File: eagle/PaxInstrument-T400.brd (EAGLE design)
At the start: 99.1 x 50.8 mm, 115 parts, among them IC1 MCP3424, J1 MICRO-SDCARD-CONNECTOR-330006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, U1 MCP9800, U3 MCP73831, U4 MIC5219-3.3V, U8 NC7S32, X1 FH12-12S-0.5SH, Y1 RESONATORSMD

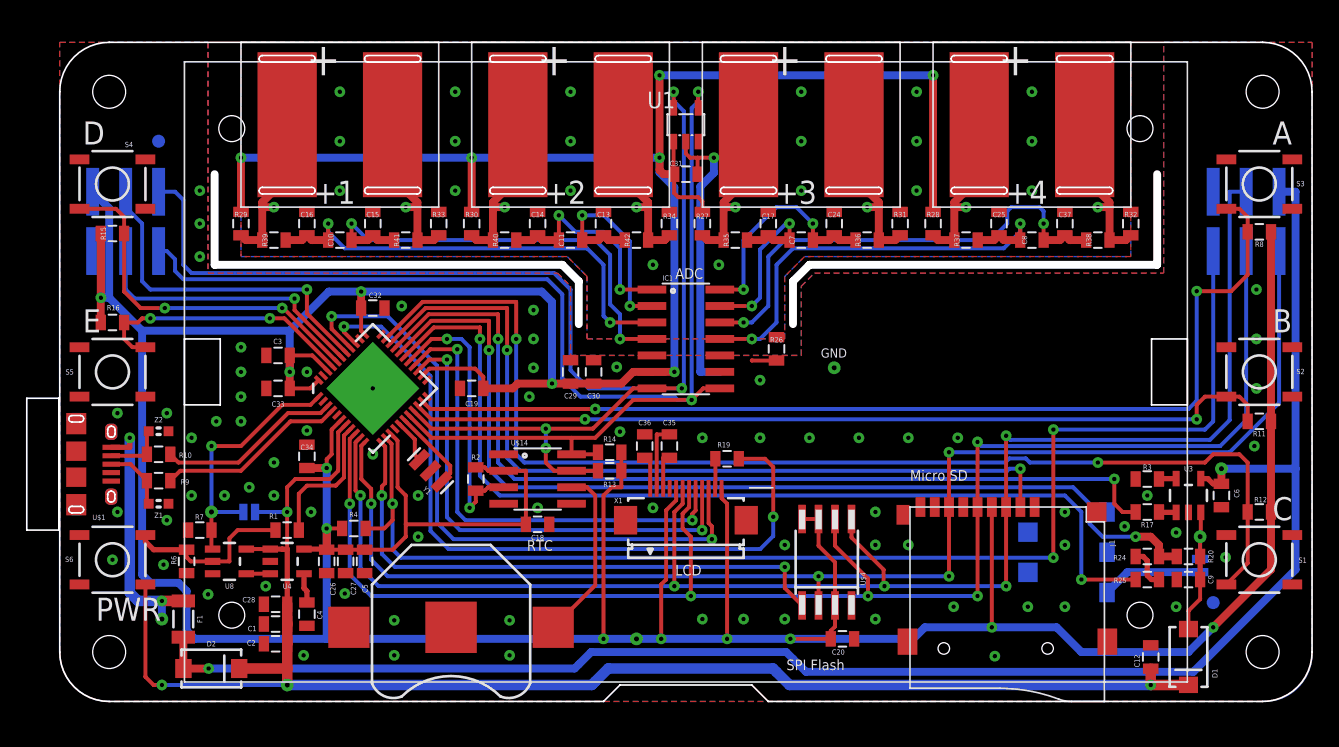
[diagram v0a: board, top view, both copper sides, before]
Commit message: Updated PCB for Rev 0.9
Updated Micro SD card position and reach enclosure edge (issue #79)
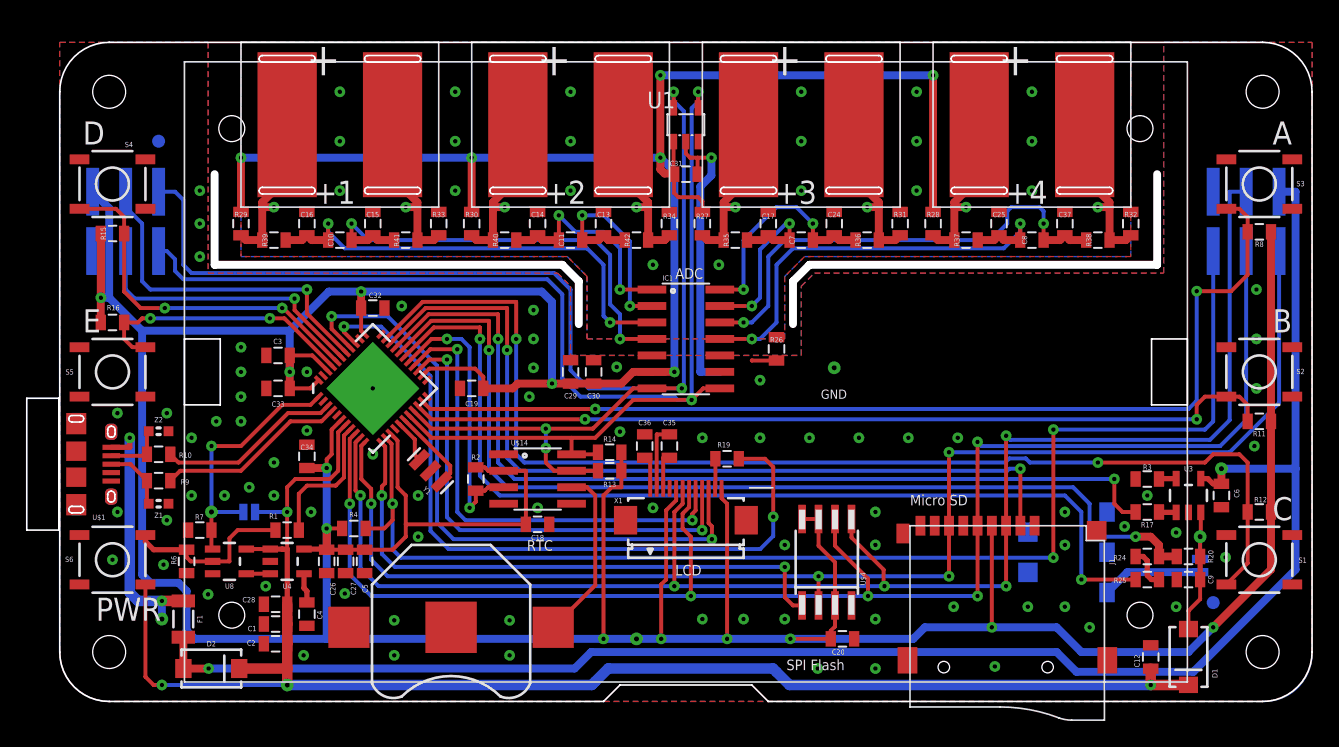
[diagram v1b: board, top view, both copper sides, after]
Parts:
- moved J1 1.44 mm to (73.0, 6.05)
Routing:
- net 3.3V: track 464.3 -> 462.7 mm
- net SD_CS: track 64.7 -> 66.1 mm
- net GND: track 24.8 -> 24.6 mm, vias 74 -> 76

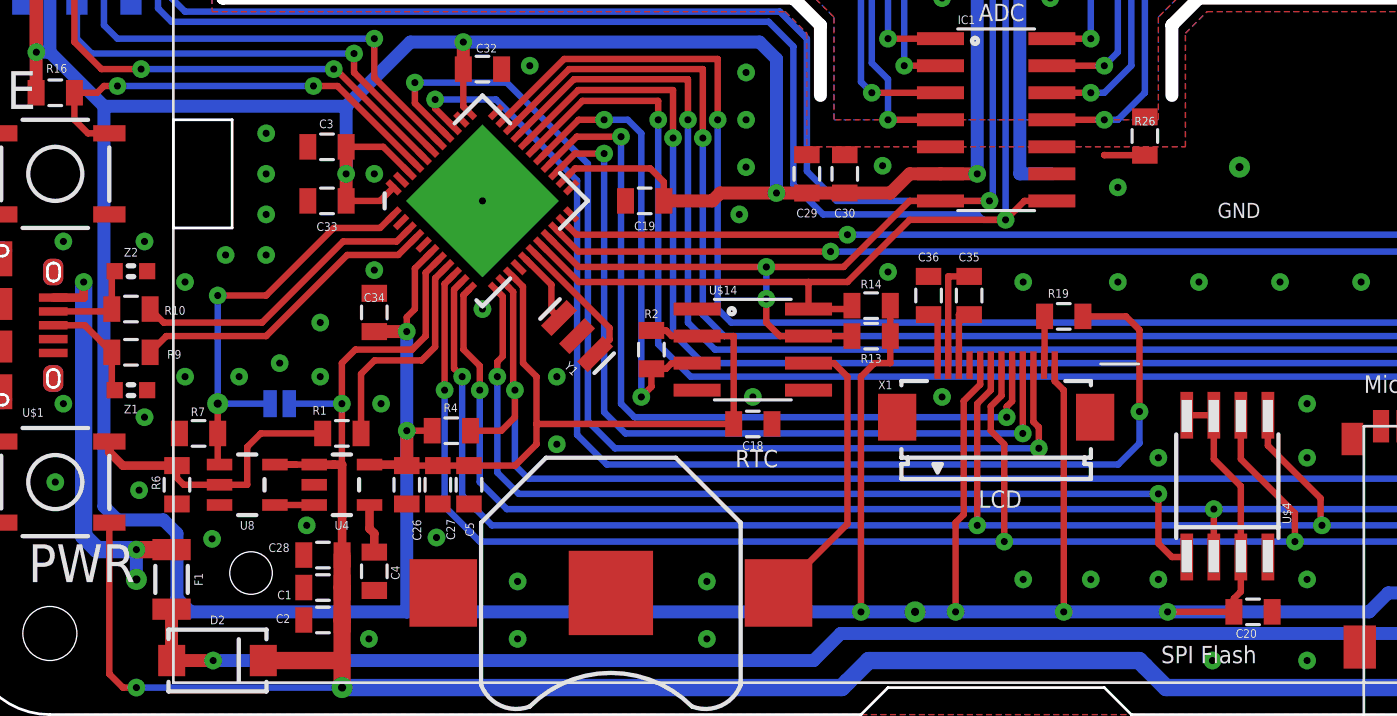
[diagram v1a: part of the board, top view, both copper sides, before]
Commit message: Updated PCB and library for Rev 0.9
- Updated test point library for both side solder mask (issue #106)
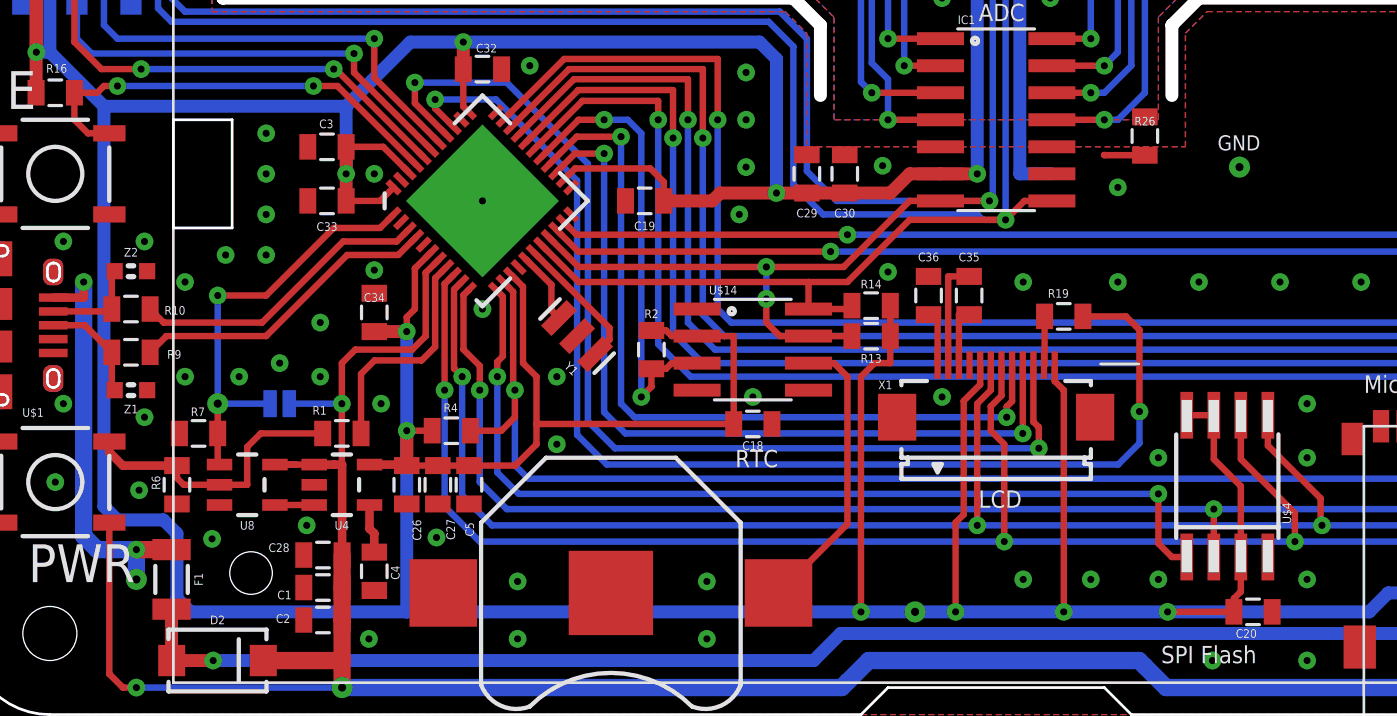
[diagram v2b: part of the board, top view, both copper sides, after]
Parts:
- TP10, TP11, TP12, TP13, TP14, TP15, TP9: device SparkFun-Passives:TP_15TH -> PaxInstrument-T400:TP_15TH
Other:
- board text added: "USBVCC"
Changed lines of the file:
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@@
 <grid distance="25" unitdist="mil" unit="mil" style="lines" multiple="1" display="yes" altdistance="6.25" altunitdist="mil" altunit="mil"/>
 <layers>
-<layer number="1" name="Top" color="4" fill="1" visible="no" active="yes"/>
+<layer number="1" name="Top" color="4" fill="1" visible="yes" active="yes"/>
 <layer number="2" name="Route2" color="1" fill="3" visible="no" active="no"/>
 <layer number="3" name="Route3" color="4" fill="3" visible="no" active="no"/>
@@
 <layer number="14" name="Route14" color="1" fill="6" visible="no" active="no"/>
 <layer number="15" name="Route15" color="4" fill="6" visible="no" active="no"/>
-<layer number="16" name="Bottom" color="1" fill="1" visible="no" active="yes"/>
-<layer number="17" name="Pads" color="2" fill="1" visible="no" active="yes"/>
-<layer number="18" name="Vias" color="2" fill="1" visible="no" active="yes"/>
+<layer number="16" name="Bottom" color="1" fill="1" visible="yes" active="yes"/>
+<layer number="17" name="Pads" color="2" fill="1" visible="yes" active="yes"/>
+<layer number="18" name="Vias" color="2" fill="1" visible="yes" active="yes"/>
 <layer number="19" name="Unrouted" color="6" fill="1" visible="yes" active="yes"/>
 <layer number="20" name="Dimension" color="13" fill="1" visible="yes" active="yes"/>
 <layer number="21" name="tPlace" color="7" fill="1" visible="yes" active="yes"/>
-<layer number="22" name="bPlace" color="14" fill="1" visible="no" active="yes"/>
+<layer number="22" name="bPlace" color="14" fill="1" visible="yes" active="yes"/>
 <layer number="23" name="tOrigins" color="15" fill="1" visible="yes" active="yes"/>
-<layer number="24" name="bOrigins" color="15" fill="1" visible="no" active="yes"/>
+<layer number="24" name="bOrigins" color="15" fill="1" visible="yes" active="yes"/>
 <layer number="25" name="tNames" color="7" fill="1" visible="no" active="yes"/>
 <layer number="26" name="bNames" color="7" fill="1" visible="no" active="yes"/>
@@
 <layer number="45" name="Holes" color="7" fill="1" visible="no" active="yes"/>
 <layer number="46" name="Milling" color="3" fill="1" visible="yes" active="yes"/>
-<layer number="47" name="Measures" color="7" fill="1" visible="yes" active="yes"/>
+<layer number="47" name="Measures" color="7" fill="1" visible="no" active="yes"/>
 <layer number="48" name="Document" color="7" fill="1" visible="yes" active="yes"/>
 <layer number="49" name="Reference" color="7" fill="1" visible="no" active="yes"/>
@@
 <text x="36.0045" y="11.6205" size="0.8128" layer="21" font="vector" ratio="15">RTC</text>
 <text x="47.4345" y="32.5755" size="0.8128" layer="21" font="vector" ratio="15">ADC</text>
-<text x="58.658" y="24.038" size="0.7112" layer="21" font="vector" ratio="15" align="top-left">GND</text>
+<text x="58.658" y="27.213" size="0.7112" layer="21" font="vector" ratio="15" align="top-left">GND</text>
 <wire x1="66.339" y1="-3.64" x2="77.339" y2="-3.64" width="0.127" layer="47"/>
 <dimension x1="66.339" y1="-3.64" x2="63.5" y2="0" x3="71.12" y3="-1.82" textsize="0.8128" layer="47" dtype="vertical" visible="yes"/>
+<text x="9.763" y="7.8455" size="0.7112" layer="22" font="vector" ratio="15" rot="MR0" align="top-left">USBVCC</text>
 </plain>
 <attributes>
@@
 <attribute name="NAME" x="3.01625" y="14.19225" size="0.4064" layer="25" align="center"/>
 </element>
-<element name="TP9" library="SparkFun-Passives" package="TP_15TH" value="PWR_ON/OFF" x="11.695" y="14.605" smashed="yes" rot="MR0">
+<element name="TP9" library="PaxInstrument-T400" package="TP_15TH" value="PWR_ON/OFF" x="11.695" y="14.605" smashed="yes" rot="MR0">
 <attribute name="MPN" value="N/A" x="11.695" y="14.605" size="1.778" layer="28" rot="MR0" display="off"/>
 <attribute name="OC_DIGIKEY" value="N/A" x="11.695" y="14.605" size="1.778" layer="28" rot="MR0" display="off"/>
@@
 </element>
 <element name="JP1" library="SparkFun-Passives" package="SJ_2S-NO" value="" x="14.605" y="14.605" rot="MR180"/>
-<element name="TP10" library="SparkFun-Passives" package="TP_15TH" value="TEST-POINTTP_15TH_THRU" x="7.874" y="6.35">
+<element name="TP10" library="PaxInstrument-T400" package="TP_15TH" value="TEST-POINTTP_15TH_THRU" x="7.874" y="6.35">
 <attribute name="MPN" value="N/A" x="7.874" y="6.35" size="1.778" layer="27" display="off"/>
 <attribute name="OC_DIGIKEY" value="N/A" x="7.874" y="6.35" size="1.778" layer="27" display="off"/>
 </element>
-<element name="TP11" library="SparkFun-Passives" package="TP_15TH" value="VBUSIN" x="89.535" y="17.93875">
+<element name="TP11" library="PaxInstrument-T400" package="TP_15TH" value="VBUSIN" x="89.535" y="17.93875">
 <attribute name="MPN" value="N/A" x="89.535" y="17.93875" size="1.778" layer="27" display="off"/>
 <attribute name="OC_DIGIKEY" value="N/A" x="89.535" y="17.93875" size="1.778" layer="27" display="off"/>
 </element>
-<element name="TP12" library="SparkFun-Passives" package="TP_15TH" value="VBUS" x="17.537" y="1.27" rot="MR0">
+<element name="TP12" library="PaxInstrument-T400" package="TP_15TH" value="VBUS" x="17.537" y="1.27" rot="MR0">
 <attribute name="MPN" value="N/A" x="17.537" y="1.27" size="1.778" layer="28" rot="MR0" display="off"/>
 <attribute name="OC_DIGIKEY" value="N/A" x="17.537" y="1.27" size="1.778" layer="28" rot="MR0" display="off"/>
 </element>
-<element name="TP13" library="SparkFun-Passives" package="TP_15TH" value="3.3V" x="44.45" y="4.826" rot="MR0">
+<element name="TP13" library="PaxInstrument-T400" package="TP_15TH" value="3.3V" x="44.45" y="4.826" rot="MR0">
 <attribute name="MPN" value="N/A" x="44.45" y="4.826" size="1.778" layer="28" rot="MR0" display="off"/>
 <attribute name="OC_DIGIKEY" value="N/A" x="44.45" y="4.826" size="1.778" layer="28" rot="MR0" display="off"/>
 </element>
-<element name="TP14" library="SparkFun-Passives" package="TP_15TH" value="VBAT" x="87.895" y="12.7025">
+<element name="TP14" library="PaxInstrument-T400" package="TP_15TH" value="VBAT" x="87.895" y="12.7025">
 <attribute name="MPN" value="N/A" x="87.895" y="12.7025" size="1.778" layer="27" display="off"/>
 <attribute name="OC_DIGIKEY" value="N/A" x="87.895" y="12.7025" size="1.778" layer="27" display="off"/>
@@
 <attribute name="NAME" x="86.625" y="11.43" size="0.4064" layer="26" rot="MR270"/>
 </element>
-<element name="TP15" library="SparkFun-Passives" package="TP_15TH" value="GND" x="59.69" y="25.7175"/>
+<element name="TP15" library="PaxInstrument-T400" package="TP_15TH" value="GND" x="59.69" y="25.7175"/>
 <element name="GND" library="PaxInstrument-T400" package="SPARKFUN-DIGITALIC_SPARKFUN-DIGITALIC_QFN-44" value="SPARKFUN-DIGITALIC_QFN_ATMEGA32U4" x="24.13" y="24.13" locked="yes" smashed="yes" rot="R45"/>
 <element name="J1" library="SeeesStudio-OPL" package="9P-SMD-W-RING" value="MICRO-SDCARD-CONNECTOR-3300060P1" x="73.025" y="6.053" locked="yes" smashed="yes" rot="R270">
@@
 <via x="7.874" y="7.75" extent="1-16" drill="0.3302"/>
 <wire x1="7.874" y1="7.75" x2="9.525" y2="7.75" width="0.8128" layer="1"/>
-<wire x1="7.874" y1="6.35" x2="7.874" y2="7.75" width="0.6096" layer="16"/>
+<wire x1="7.874" y1="6.35" x2="7.874" y2="7.75" width="0.8128" layer="16"/>
 </signal>
 <signal name="D-">

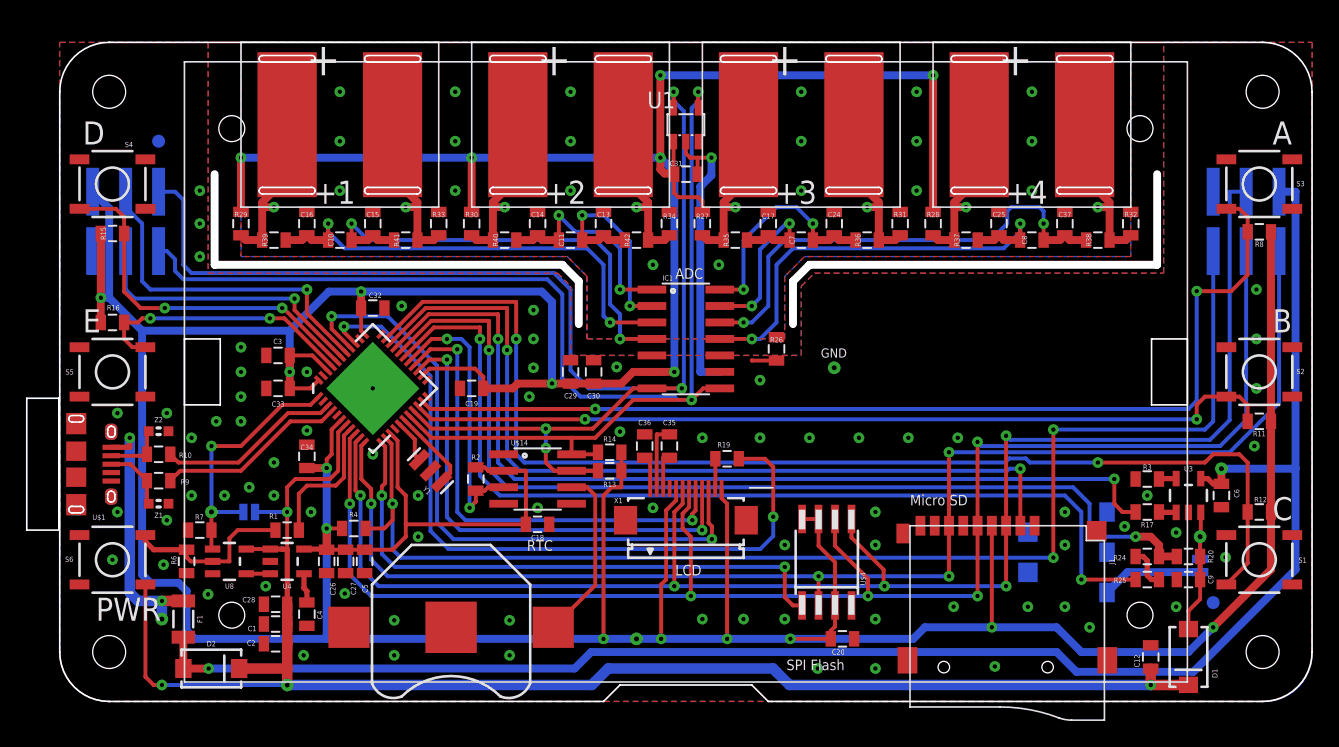
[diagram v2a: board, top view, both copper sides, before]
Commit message: Updated PCB and Library for Rev 0.9
- Update test hook dill size for test hook (issue #38)
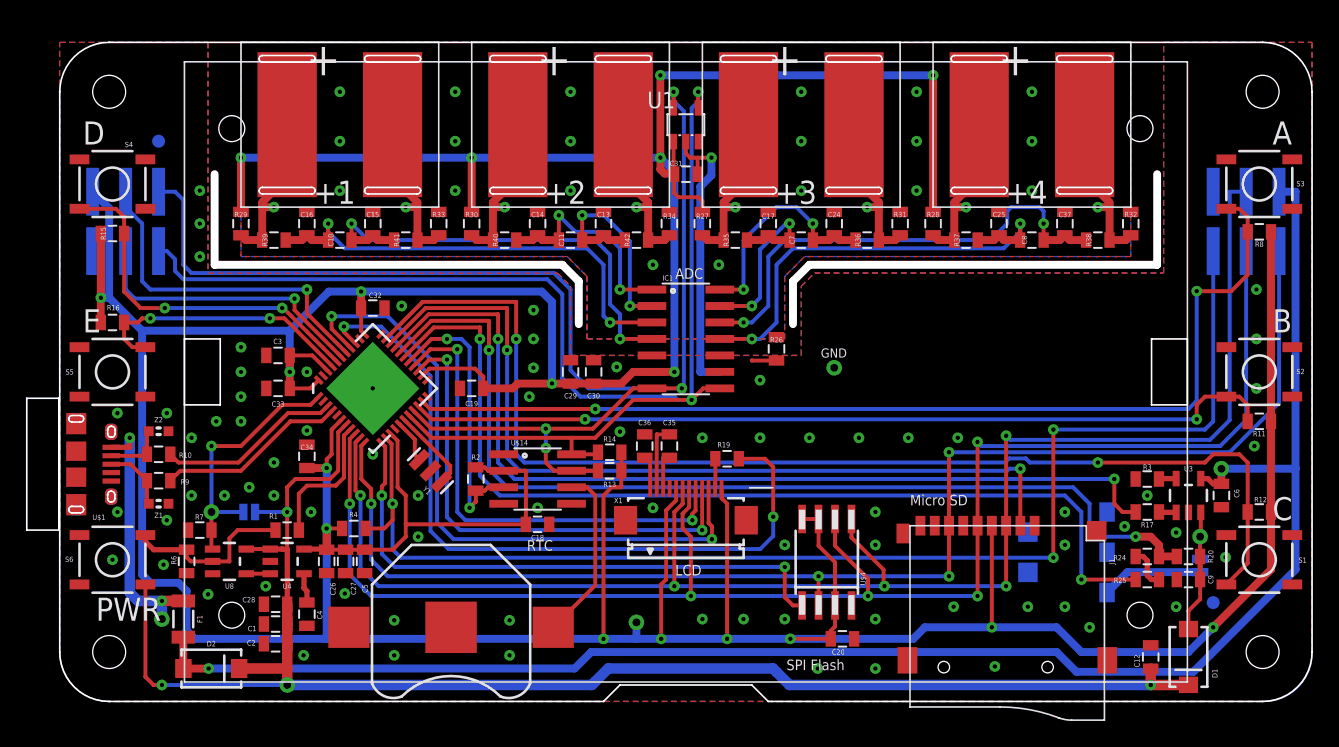
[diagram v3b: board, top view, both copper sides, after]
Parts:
- moved TP13 1.27 mm to (44.5, 6.10)
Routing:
- net 3.3V: track 462.7 -> 463.9 mm
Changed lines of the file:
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@@
 <text x="78.105" y="-6.64" size="0.6096" layer="47" align="center-left">Card dashing position</text>
 <text x="60.563" y="27.213" size="0.7112" layer="22" font="vector" ratio="15" rot="MR0" align="top-left">GND</text>
-<text x="45.323" y="3.718" size="0.7112" layer="22" font="vector" ratio="15" rot="MR0" align="top-left">3.3V</text>
+<text x="45.323" y="4.988" size="0.7112" layer="22" font="vector" ratio="15" rot="MR0" align="top-left">3.3V</text>
 <text x="90.408" y="17.053" size="0.7112" layer="22" font="vector" ratio="15" rot="MR0" align="top-left">VBUS_IN</text>
 <text x="89.138" y="14.1955" size="0.7112" layer="22" font="vector" ratio="15" rot="MR0" align="top-left">VBAT</text>
@@
 <attribute name="OC_DIGIKEY" value="N/A" x="17.537" y="1.27" size="1.778" layer="28" rot="MR0" display="off"/>
 </element>
-<element name="TP13" library="PaxInstrument-T400" package="TP_15TH" value="3.3V" x="44.45" y="4.826" rot="MR0">
-<attribute name="MPN" value="N/A" x="44.45" y="4.826" size="1.778" layer="28" rot="MR0" display="off"/>
-<attribute name="OC_DIGIKEY" value="N/A" x="44.45" y="4.826" size="1.778" layer="28" rot="MR0" display="off"/>
+<element name="TP13" library="PaxInstrument-T400" package="TP_15TH" value="3.3V" x="44.45" y="6.096" rot="MR0">
+<attribute name="MPN" value="N/A" x="44.45" y="6.096" size="1.778" layer="28" rot="MR0" display="off"/>
+<attribute name="OC_DIGIKEY" value="N/A" x="44.45" y="6.096" size="1.778" layer="28" rot="MR0" display="off"/>
 </element>
 <element name="TP14" library="PaxInstrument-T400" package="TP_15TH" value="VBAT" x="87.895" y="12.7025">
@@
 <contactref element="GND" pad="24"/>
 <via x="51.435" y="4.826" extent="1-16" drill="0.3302"/>
-<wire x1="44.45" y1="4.826" x2="41.91" y2="4.826" width="0.6096" layer="16"/>
 <wire x1="51.435" y1="4.826" x2="46.355" y2="4.826" width="0.6096" layer="16"/>
 <via x="88.9" y="5.715" extent="1-16" drill="0.3302"/>
-<wire x1="46.355" y1="4.826" x2="44.45" y2="4.826" width="0.6096" layer="16"/>
 <wire x1="86.995" y1="3.81" x2="88.9" y2="5.715" width="0.6096" layer="16"/>
 <wire x1="35.93" y1="17.78" x2="34.2138" y2="17.78" width="0.3048" layer="1"/>
@@
 <wire x1="46.609" y1="40.69" x2="46.2915" y2="41.0075" width="0.6096" layer="1"/>
 <wire x1="46.2915" y1="41.0075" x2="46.2915" y2="41.91" width="0.6096" layer="1"/>
+<wire x1="46.355" y1="4.826" x2="44.45" y2="4.826" width="0.6096" layer="16"/>
+<wire x1="44.45" y1="4.826" x2="41.91" y2="4.826" width="0.6096" layer="16"/>
+<wire x1="44.45" y1="6.096" x2="44.45" y2="4.826" width="0.6096" layer="16"/>
 </signal>
 <signal name="3V3EN">
